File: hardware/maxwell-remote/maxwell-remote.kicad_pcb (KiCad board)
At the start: 2 copper layers, 77.5 x 38.1 mm, 46 parts, among them J1 INPUT, J2 UART, J3 Left, J4 Right, J5 Programmer, J6 B0_JMP, J7 B1_JMP, J8 SPI2, J9 ESP_BM, Q2 NDS332P, Q4 NDS332P, U1 STM32F103C8Tx, U2 ESP32-WROOM, U3 MIC5209-ADJ, U5 SN65HVD235, U8 OLED-SSD1306, Y1 Crystal, Y2 Crystal_GND23

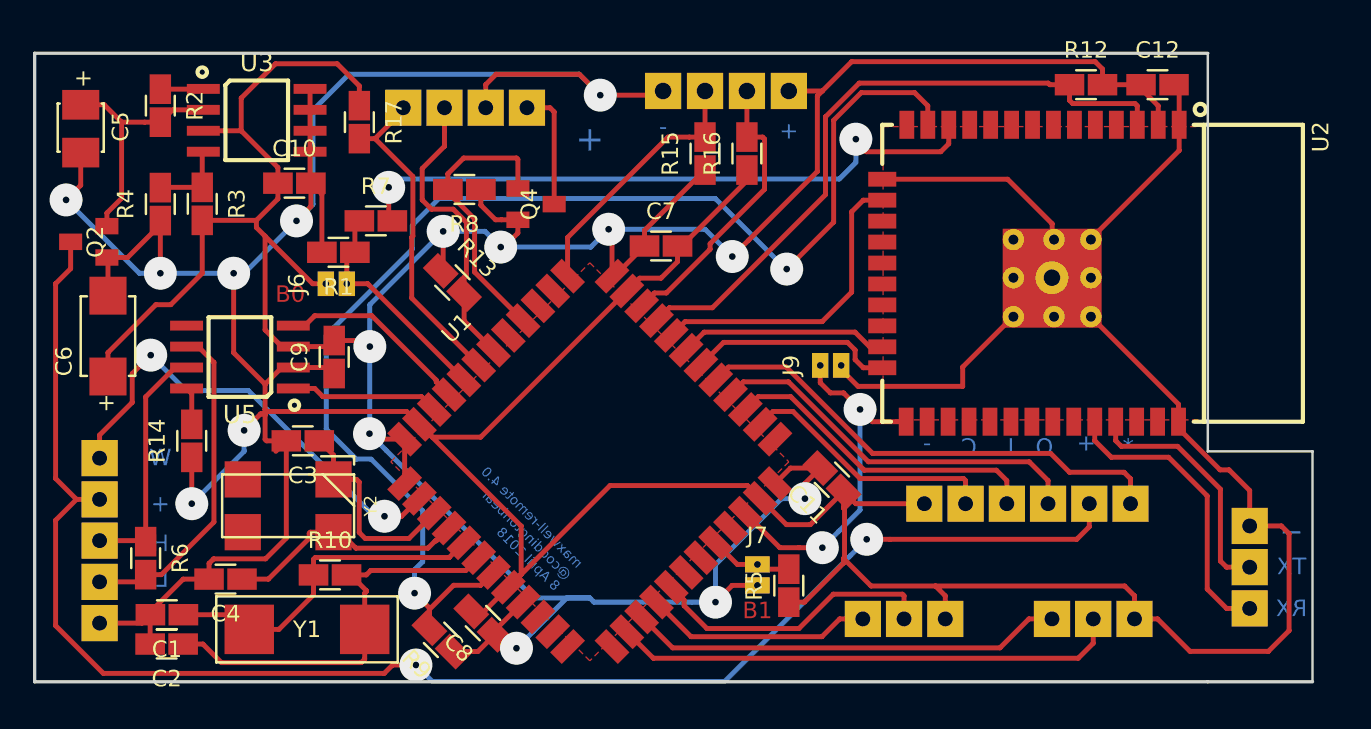
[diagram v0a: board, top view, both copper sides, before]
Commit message: Updating to multi-board linked by FPC connectors.
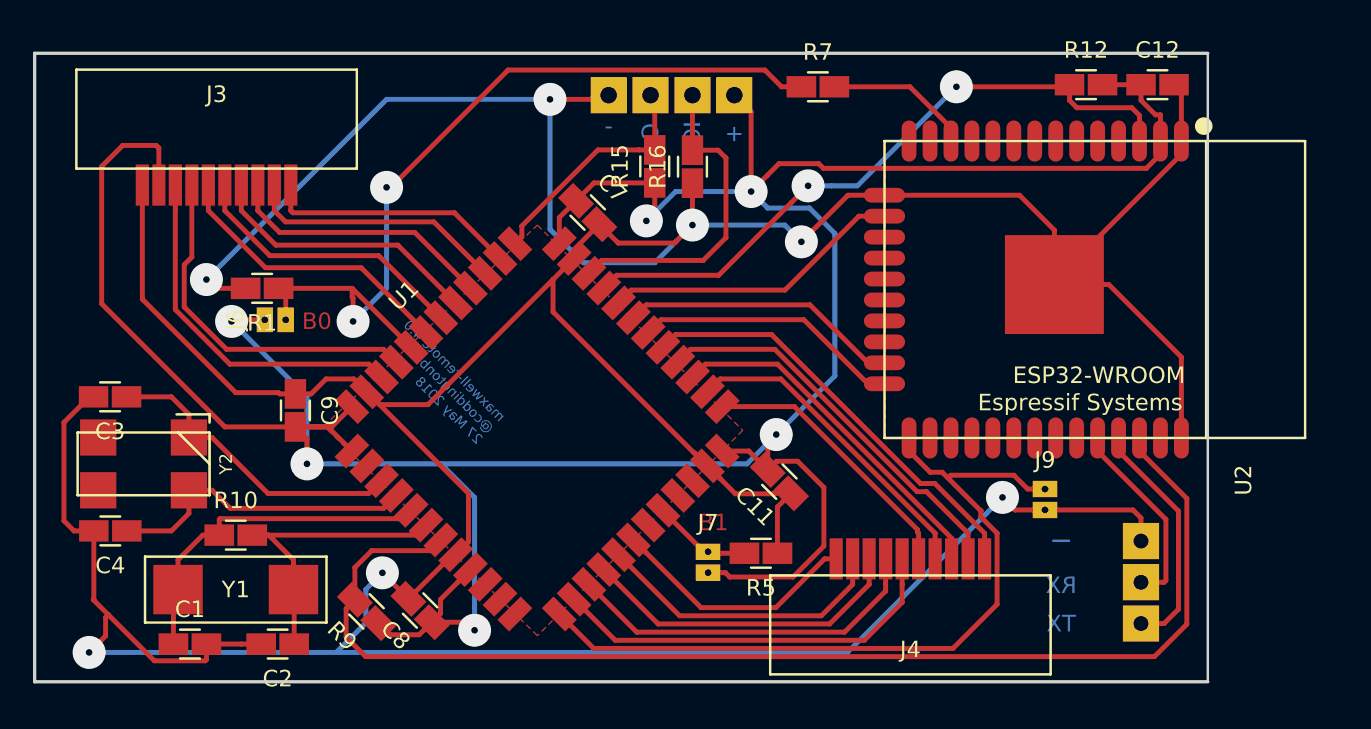
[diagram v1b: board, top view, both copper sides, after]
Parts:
- removed C10: 0.1u, coddingtonbear/coddingtonbear.pretty:0805_Milling
- removed C5: 1u, celeritous/KiCad.pretty:CAPACITOR_TANTALUM_B
- removed C6: 2.2u, celeritous/KiCad.pretty:CAPACITOR_TANTALUM_C
- removed J1: INPUT, coddingtonbear:JST_XH_B05B-XH-A_05x2.50mm_Straight_LargePads
- removed J8: SPI2, coddingtonbear:JST_XH_B06B-XH-A_06x2.50mm_Straight_LargePads
- removed Q2, Q4: NDS332P, cvra/kicad-lib/footprints/_std.pretty:SSOT-3
- removed R13, R17: 2.2k, coddingtonbear/coddingtonbear.pretty:0805_Milling
- removed R14, R2, R8: 10k, coddingtonbear/coddingtonbear.pretty:0805_Milling
- removed R3: 60k, coddingtonbear/coddingtonbear.pretty:0805_Milling
- removed R4: 100k, coddingtonbear/coddingtonbear.pretty:0805_Milling
- removed R6: 120, coddingtonbear/coddingtonbear.pretty:0805_Milling
- removed U3: MIC5209-ADJ, OLIMEX/KiCAD/KiCAD_Footprints/OLIMEX_IC-FP.pretty:SOIC-8_208mil
- removed U5: SN65HVD235, OLIMEX/KiCAD/KiCAD_Footprints/OLIMEX_IC-FP.pretty:SOIC-8_208mil
- removed U8: OLED-SSD1306, coddingtonbear:JST_XH_B04B-XH-A_04x2.50mm_Straight_LargePads
- J3: value Left -> FPC 1; footprint coddingtonbear:JST_XH_B03B-XH-A_03x2.50mm_Straight_LargePads -> coddingtonbear/coddingtonbear.pretty:10P_FPC_1.0mm; moved to F.Cu
- J4: value Right -> FPC 2; footprint coddingtonbear:JST_XH_B03B-XH-A_03x2.50mm_Straight_LargePads -> coddingtonbear/coddingtonbear.pretty:10P_FPC_1.0mm; moved to F.Cu
- U2: footprint OLIMEX/KiCAD/KiCAD_Footprints/OLIMEX_Cases-FP.pretty:ESP-WROOM-32_MODULE -> NorbotNorway/NorBotKiCadFootprints.pretty:ESP32-WROOM
- moved J3 51.4 mm to (108.8, 63.9)
- moved R7 28.0 mm to (145.3, 57.9)
- moved J9 15.5 mm to (159.0, 82.3), turned to 0 degrees
- moved J4 14.1 mm to (150.9, 86.5), turned to 0 degrees
- moved C3 12.0 mm to (102.4, 76.7)
- moved Y2 9.12 mm to (104.4, 80.8)
- moved C4 7.57 mm to (102.4, 84.8)
- moved C2 6.73 mm to (112.5, 91.7)
- moved J2 6.65 mm to (164.9, 90.5)
- moved R10 6.20 mm to (110.0, 85.1)
- moved R1 5.12 mm to (111.6, 70.1)
- moved Y1 4.95 mm to (110.0, 88.4)
- moved C7 4.89 mm to (131.3, 65.5), turned to 315 degrees
- moved R9 4.83 mm to (117.9, 89.7)
- moved J6 4.30 mm to (111.7, 72.0)
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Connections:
- J2 pad 1: BT_IN -> BT_OUT
- J2 pad 2: BT_OUT -> BT_IN
- J3 pad 2: ~LEFT_A -> +3V3
- J3 pad 3: ~LEFT_B -> CAN_TX
- J4 pad 1: GND -> ~ENABLE_SCREEN
- J4 pad 2: ~RIGHT_A -> SCREEN_A0
- J4 pad 3: ~RIGHT_B -> ~SCREEN_RST
- U1 pad 13: Net-(U1-Pad13) -> ESP_BOOT_MODE
- U1 pad 14: ~RIGHT_A -> ~RIGHT_B
- U1 pad 15: ~RIGHT_B -> ~RIGHT_A
- U1 pad 18: Net-(U1-Pad18) -> WAKE
- U1 pad 2: WAKE -> Net-(U1-Pad2)
- U1 pad 22: ESP_BOOT_MODE -> Net-(U1-Pad22)
- U1 pad 25: Net-(U1-Pad25) -> ~SPI1_CS_4
- U1 pad 26: Net-(J8-Pad5) -> ~SCREEN_CS
- U1 pad 27: Net-(J8-Pad4) -> ~SCREEN_RST
- U1 pad 28: Net-(J8-Pad3) -> SCREEN_A0
- U1 pad 29: SPI_CS -> ~ENABLE_SCREEN
- U1 pad 38: Net-(U1-Pad38) -> ~ENABLE_SCREEN_BACKLIGHT
- U1 pad 39: Net-(U1-Pad39) -> SPI1_SCK
- U1 pad 40: ~ENABLE_SCREEN -> SPI1_MISO
- U1 pad 41: Net-(U1-Pad41) -> SPI1_MOSI
- U1 pad 42: SCL -> ~SPI1_CS_3
- U1 pad 43: SDA -> ~SPI1_CS_2
- U2 pad 13: NRST -> Net-(U2-Pad13)
- U2 pad 36: Net-(U2-Pad36) -> NRST
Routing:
- net +BATT: track 95.9 -> 0.00 mm, vias 2 -> 0
- net BOOT0: track 13.6 -> 51.1 mm, vias 0 -> 2
- net Net-(R7-Pad2): track 39.9 -> 8.90 mm, vias 2 -> 0
- net SPI_CS: track 29.8 -> 0.00 mm
- net ESP_BOOT_MODE: track 22.1 -> 47.6 mm, vias 2 -> 0
- net GND: track 333.0 -> 308.8 mm
- net SCREEN_A0: track 0.00 -> 24.1 mm
- net Net-(J8-Pad3): track 23.5 -> 0.00 mm
- net ~SCREEN_RST: track 0.00 -> 21.6 mm
- net CAN-: track 20.2 -> 0.00 mm
- net SDA: track 19.9 -> 0.00 mm
- net Net-(J8-Pad4): track 19.7 -> 0.00 mm
- net ~SCREEN_CS: track 0.00 -> 19.6 mm
- net SCL: track 17.9 -> 0.00 mm
- net ~SPI1_CS_2: track 0.00 -> 17.8 mm
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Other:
- board size 77.5 x 38.1 mm -> 71.1 x 38.1 mm
- board text added: "maxwell-remote 4.0 @coddingtonbear 27 May 2018"
- board text removed: "*"
- board text removed: "H"
- board text removed: "I"
- board text removed: "L"
- board text removed: "O"
- board text removed: "W"
- board text removed: "maxwell-remote 4.0 @coddingtonbear 8 April 2018"

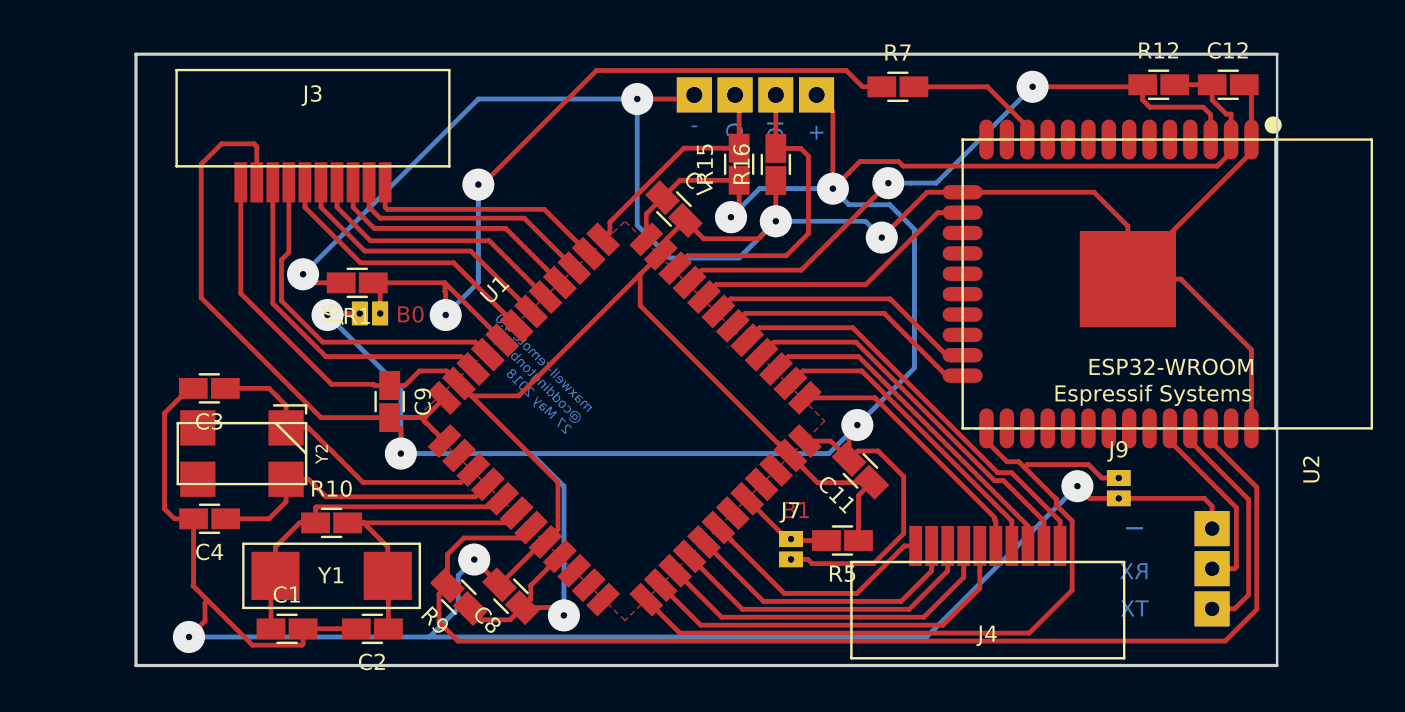
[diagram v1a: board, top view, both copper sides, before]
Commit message: Updating to v5.0 of the remote's main PCB.
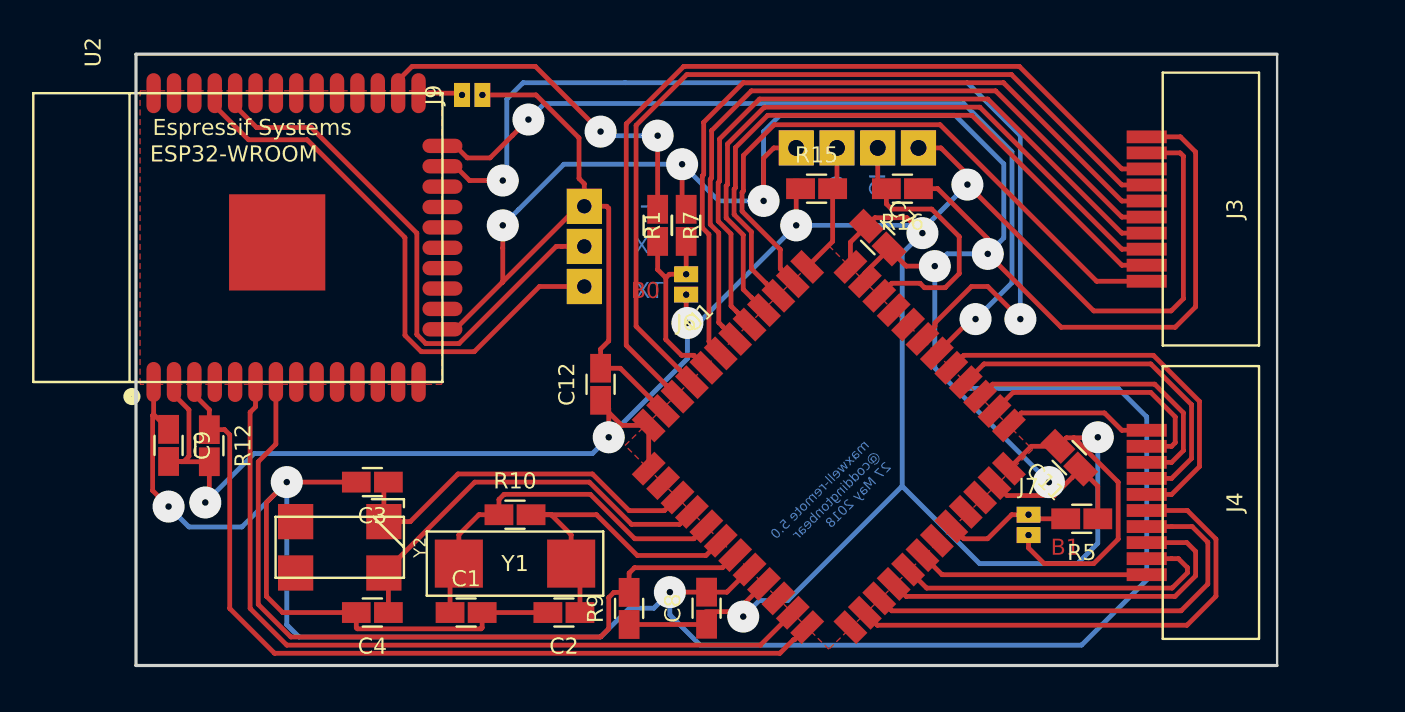
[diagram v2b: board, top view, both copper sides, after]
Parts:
- moved R12 63.3 mm to (102.4, 80.3), turned to 270 degrees
- moved U2 58.0 mm to (104.1, 67.3), turned to 270 degrees
- moved J3 52.0 mm to (160.8, 65.5), turned to 90 degrees
- moved J9 47.4 mm to (118.1, 58.4), turned to 90 degrees
- moved J2 44.0 mm to (125.7, 70.4)
- moved C12 43.3 mm to (126.7, 76.5), turned to 90 degrees
- moved R1 20.8 mm to (132.1, 66.5), turned to 90 degrees
- moved J6 20.4 mm to (132.1, 70.9), turned to 180 degrees
- moved R7 17.3 mm to (130.3, 66.5), turned to 270 degrees
- moved R5 15.0 mm to (156.7, 84.8)
- moved J7 14.9 mm to (153.4, 84.6)
- moved C9 14.0 mm to (99.8, 80.3)
- moved C11 13.0 mm to (156.0, 81.0)
- moved U1 12.8 mm to (141.0, 83.1)
- moved C7 12.8 mm to (144.0, 67.3)
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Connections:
- R7 pad 1: BOOT0 -> Net-(R7-Pad1)
- R7 pad 2: Net-(R7-Pad2) -> BOOT0
- U1 pad 11: Net-(U1-Pad11) -> BT_KEY
- U1 pad 12: Net-(U1-Pad12) -> DISBABLE_BLUETOOTH_
- U1 pad 13: ESP_BOOT_MODE -> Net-(U1-Pad13)
- U1 pad 25: ~SPI1_CS_4 -> ~ENABLE_SCREEN
- U1 pad 26: ~SCREEN_CS -> SCREEN_A0
- U1 pad 28: SCREEN_A0 -> ~SCREEN_CS
- U1 pad 29: ~ENABLE_SCREEN -> ~SPI1_CS_4
- U1 pad 32: BT_KEY -> Net-(U1-Pad32)
- U1 pad 33: DISBABLE_BLUETOOTH_ -> Net-(U1-Pad33)
- U2 pad 12: Net-(R7-Pad2) -> Net-(U2-Pad12)
- U2 pad 16: BT_KEY -> Net-(U2-Pad16)
- U2 pad 25: ESP_BOOT_MODE -> Net-(U2-Pad25)
- U2 pad 26: Net-(U2-Pad26) -> Net-(R7-Pad1)
- U2 pad 36: NRST -> Net-(U2-Pad36)
- U2 pad 6: Net-(U2-Pad6) -> BT_KEY
- U2 pad 7: Net-(U2-Pad7) -> NRST
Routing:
- net MC_IN: track 17.0 -> 63.0 mm, vias 0 -> 2
- net ESP_BOOT_MODE: track 47.6 -> 2.76 mm
- net BOOT0: track 51.1 -> 13.0 mm, vias 2 -> 0
- net MC_OUT: track 16.3 -> 53.1 mm, vias 0 -> 2
- net CAN_TX: track 21.7 -> 54.9 mm
- net CAN_RX: track 21.8 -> 53.4 mm
- net BT_KEY: track 18.3 -> 49.9 mm
- net ~SPI1_CS_2: track 17.8 -> 46.6 mm
- net ~SPI1_CS_3: track 17.3 -> 45.1 mm
- net SPI1_MOSI: track 16.9 -> 43.5 mm
- net NRST: track 75.1 -> 48.8 mm
- net SPI1_MISO: track 16.4 -> 42.1 mm
- net SPI1_SCK: track 15.9 -> 40.7 mm
- net ~ENABLE_SCREEN_BACKLIGHT: track 15.4 -> 39.2 mm
- net Net-(R7-Pad1): track 0.00 -> 23.7 mm, vias 0 -> 2
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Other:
- board text added: "maxwell-remote 5.0 @coddingtonbear 27 May 2018"
- board text removed: "maxwell-remote 4.0 @coddingtonbear 27 May 2018"

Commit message: Adding new FPC-connected board for extra connectors, can transceiver, voltage regulator.
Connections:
- J4 pad 1: ~ENABLE_SCREEN -> ~SPI_CS_5
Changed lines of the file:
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@@
     (zones 0)
     (modules 28)
-    (nets 74)
+    (nets 75)
   )
   (page A4)
@@
   (net 72 "Net-(R7-Pad1)")
   (net 73 "Net-(U2-Pad12)")
+  (net 74 ~SPI_CS_5)
   (net_class Default "This is the default net class."
     (clearance 0.195)
@@
     (add_net ~SPI1_CS_3)
     (add_net ~SPI1_CS_4)
+    (add_net ~SPI_CS_5)
   )
   (module coddingtonbear/coddingtonbear.pretty:10P_FPC_1.0mm (layer F.Cu)
@@
       (net 64 SCREEN_A0))
     (pad 1 smd rect (at 4.5 0 90) (size 0.8 2.5) (layers F.Cu F.Paste F.Mask)
-      (net 19 ~ENABLE_SCREEN))
+      (net 74 ~SPI_CS_5))
   )
   (module NorbotNorway/NorBotKiCadFootprints.pretty:ESP32-WROOM (layer F.Cu)

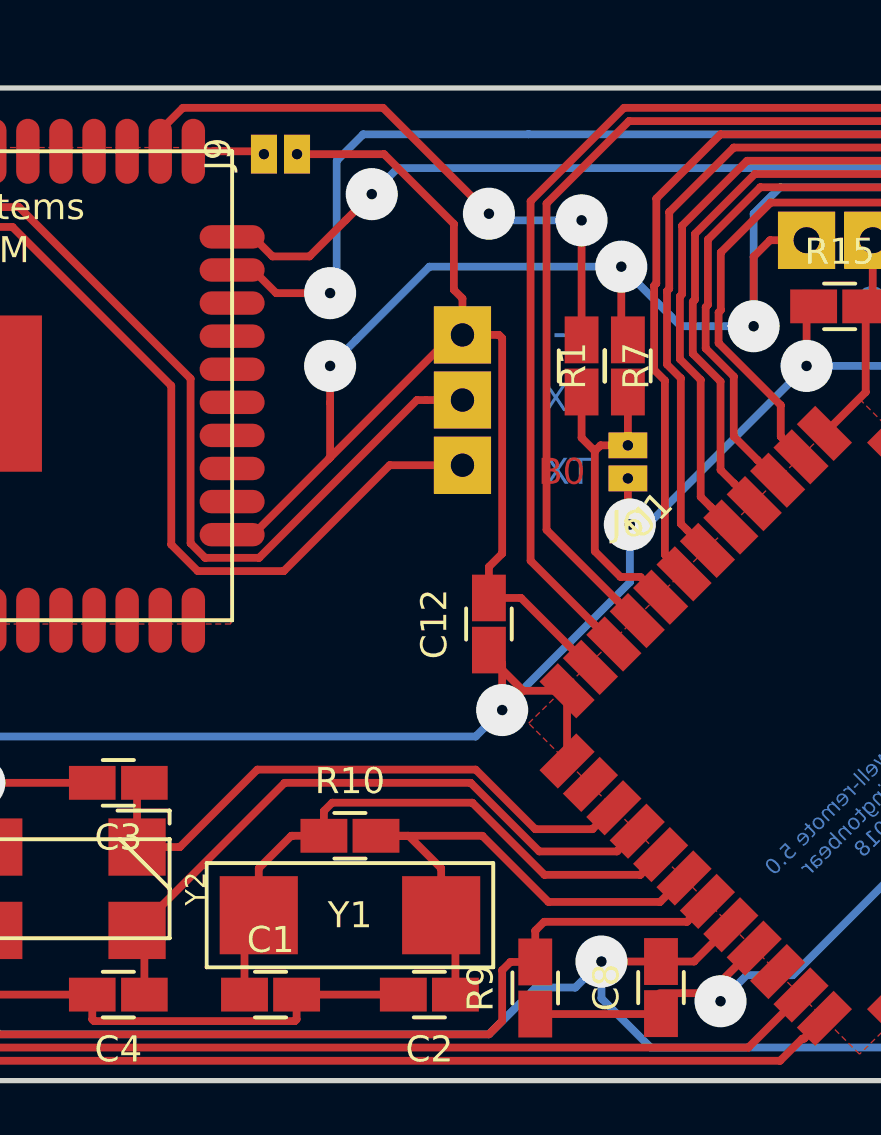
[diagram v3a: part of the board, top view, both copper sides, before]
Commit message: Finishing-up secondary connector board.
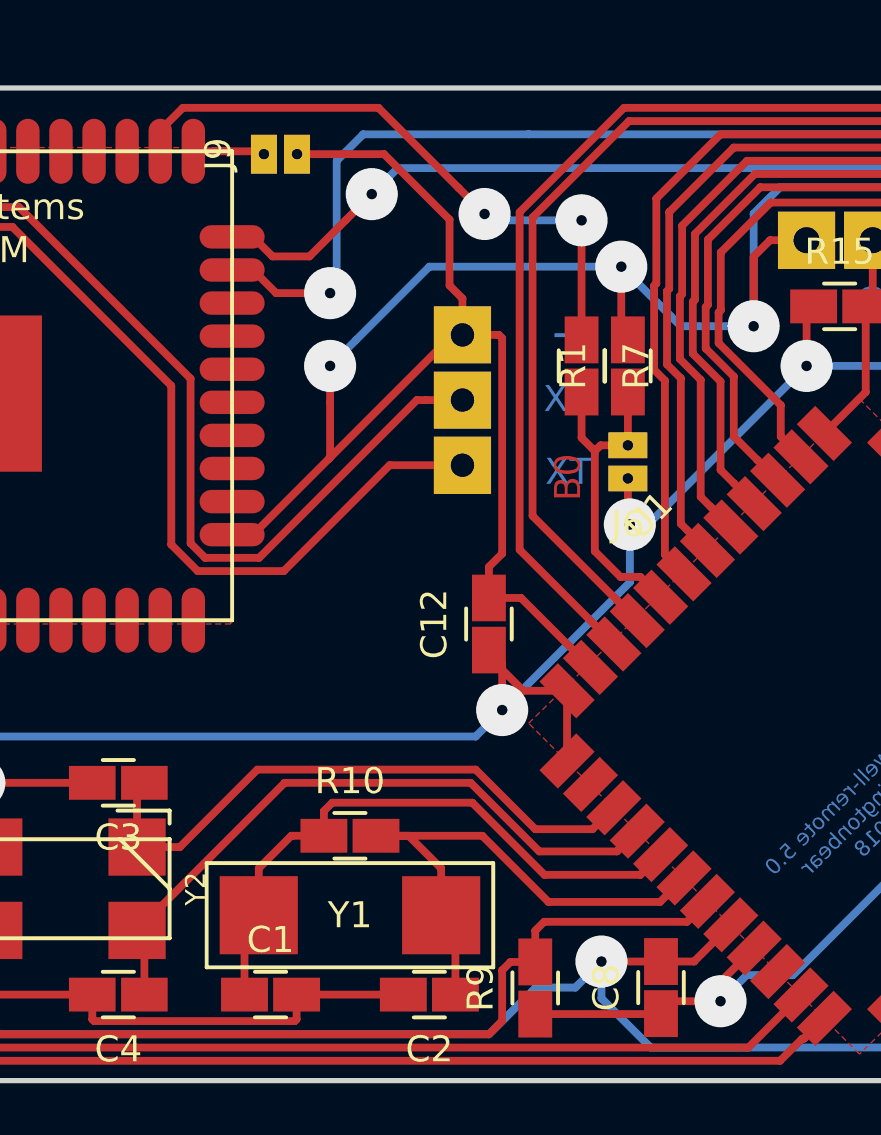
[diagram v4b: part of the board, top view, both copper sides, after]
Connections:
- net ~SPI1_CS_4 renamed ~ENABLE_CAN
- J3 pad 10: ~ENABLE_SCREEN_BACKLIGHT -> ~ENABLE_SCREEN
- J4 pad 1: ~SPI_CS_5 -> ~SPI_CS_4
- U1 pad 25: ~ENABLE_SCREEN -> ~SPI_CS_4
- U1 pad 38: ~ENABLE_SCREEN_BACKLIGHT -> ~ENABLE_SCREEN
- U2 pad 25: Net-(U2-Pad25) -> ESP_BOOT_MODE
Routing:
- net ~ENABLE_SCREEN_BACKLIGHT: track 39.2 -> 0.00 mm
- net ~ENABLE_SCREEN: track 9.36 -> 39.2 mm
- net ~SPI_CS_4: track 0.00 -> 9.36 mm

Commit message: Updating for manufacture.
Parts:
- U1: footprint kicad-castellated-breakouts:QFP48-1.27MM-CASTELLATED -> kicad-castellated-breakouts:QFP48-1.27MM-CASTELLATED-VERS
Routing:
- net GND: track 316.1 -> 350.5 mm
- net +3V3: track 203.8 -> 236.7 mm
- net Net-(U1-Pad13): track 0.00 -> 6.83 mm
- net Net-(U1-Pad2): track 0.00 -> 6.83 mm
- net SWCLK: track 8.18 -> 15.0 mm
- net ~ENABLE_SCREEN: track 39.2 -> 45.9 mm
- net ~RIGHT_B: track 31.6 -> 38.3 mm
- net DISBABLE_BLUETOOTH_: track 53.4 -> 60.1 mm
- net ~SPI_CS_4: track 9.36 -> 16.0 mm
- net BT_KEY: track 49.9 -> 56.2 mm
- net CAN_TX: track 55.2 -> 61.6 mm
- net Net-(C3-Pad1): track 23.4 -> 29.7 mm
- net SCREEN_A0: track 15.9 -> 22.1 mm
- net SPI1_SCK: track 40.7 -> 46.8 mm
- net ~RIGHT_A: track 28.3 -> 34.2 mm
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- added copper zone on B.Cu, net GND
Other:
- board text added: "maxwell-remote v5.0 @coddingtonbear 24 June 2018"
- board text removed: "maxwell-remote 5.0 @coddingtonbear 27 May 2018"
